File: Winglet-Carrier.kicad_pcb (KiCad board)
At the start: 4 copper layers, 80 x 60 mm, 69 parts, among them J1 1775862-2, J2 USB4105-GF-A-060, J3 USB4105-GF-A-060, J4 Pins_2.54_1x2, J5 Pins_2.54_1x2, M1 Mount_M3, M2 Mount_M3, M3 Mount_M3, M4 Mount_M3, M5 MM60-EZH039-B5-R850, Q1 2N7002-7-F, U1 USBLC6-2SC6, U2 USBLC6-2SC6, U3 STM32F072CxUx, U4 AP22804AW5-7, U5 AP62301WU-7, Y1 ECS-160-10-37-RWM-TR

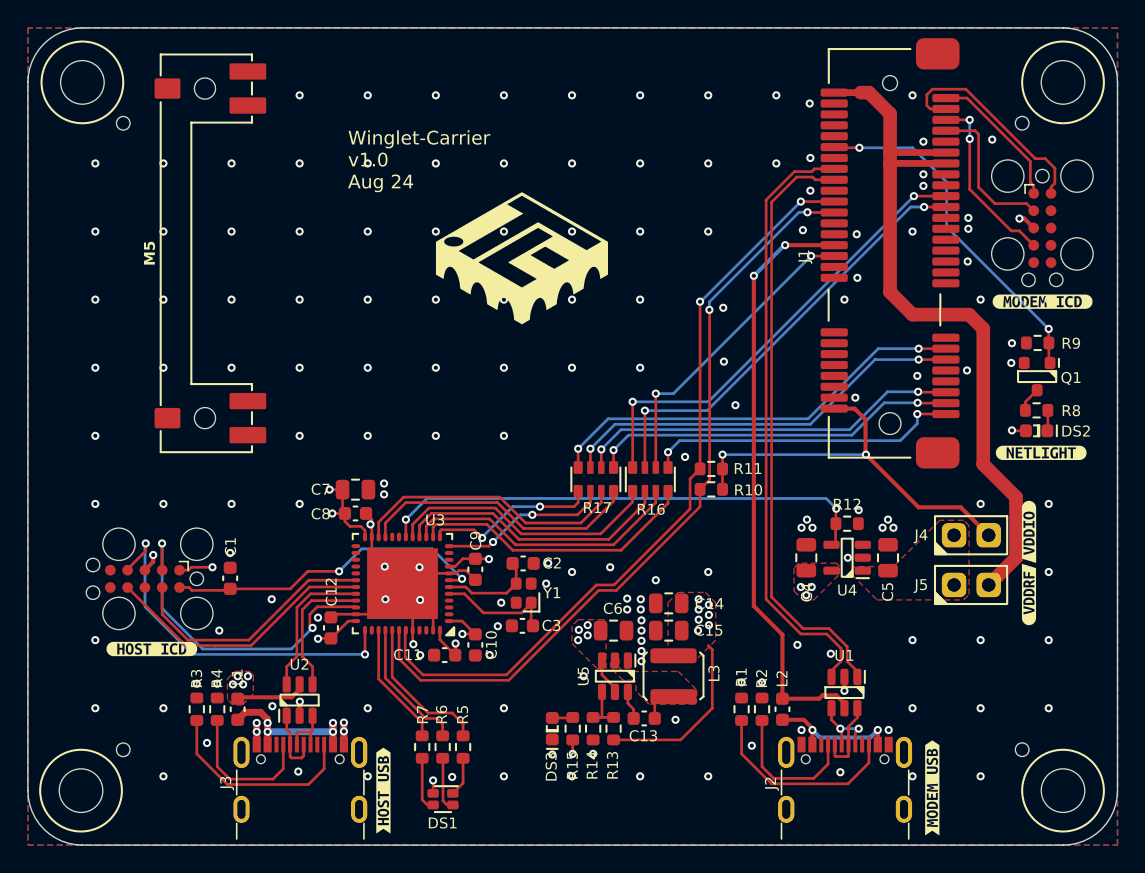
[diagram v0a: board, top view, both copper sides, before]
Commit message: Reannotate components
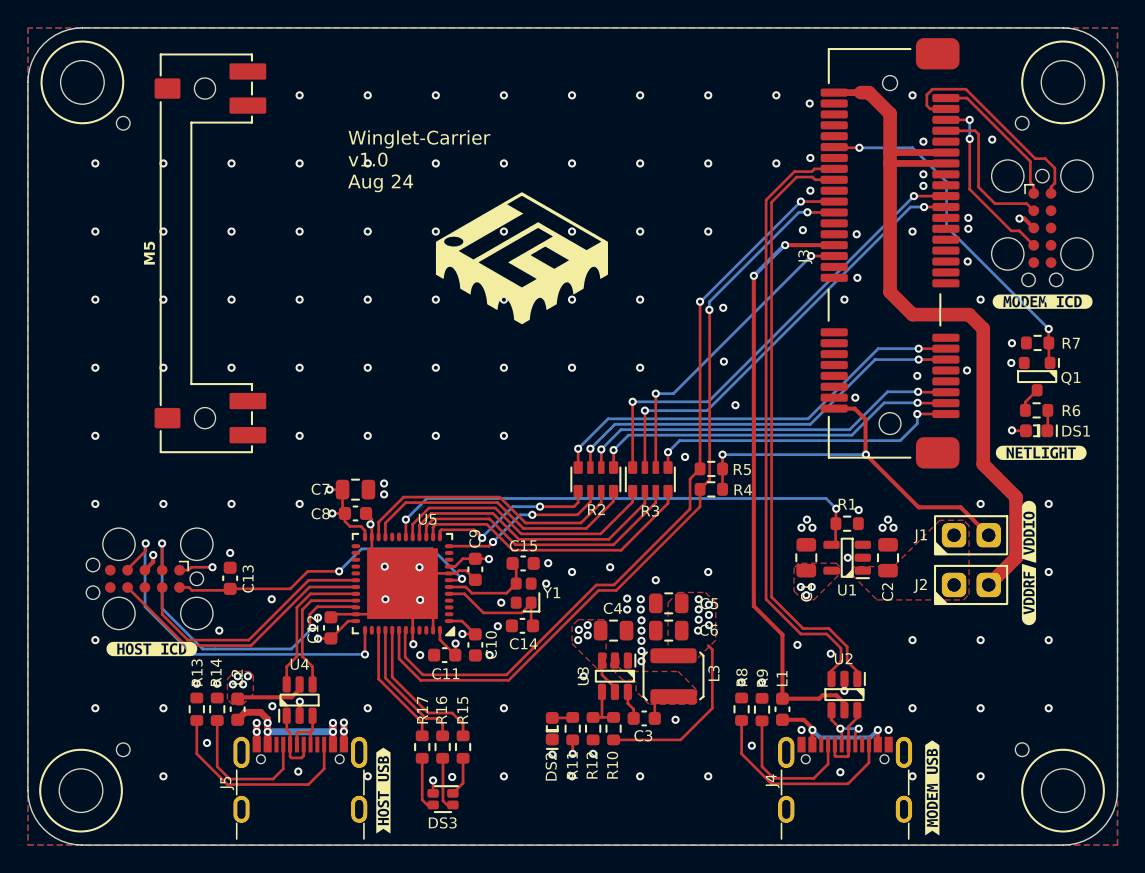
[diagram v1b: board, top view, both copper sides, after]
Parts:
- removed the J2 at (110.0, 106.3)
- removed the R1 at (102.4, 100.0)
- removed the R2 at (103.9, 100.0)
- removed the U1 at (110.0, 98.8)
- added J4: USB4105-GF-A-060, J_Connector:USB_C_USB4105-GF-A-060, F.Cu at (110.0, 106.3)
- added R8: 5K1, R_Resistor:R_0603, F.Cu at (102.4, 100.0)
- added R9: 5K1, R_Resistor:R_0603, F.Cu at (103.9, 100.0)
- added U2: USBLC6-2SC6, U_IC:SOT23_6, F.Cu at (110.0, 99.0)
- renumbered C4 to C1, C1 to C13, C3 to C14, C2 to C15, C5 to C2, C13 to C3, C6 to C4, C14 to C5, C15 to C6, DS2 to DS1, DS3 to DS2, DS1 to DS3, J4 to J1, J5 to J2, J1 to J3, J3 to J5, L2 to L1, L1 to L2, N3 to N1, N4 to N2, N5 to N3, N6 to N4, N1 to N5, N2 to N6, R12 to R1, R13 to R10, R15 to R11, R14 to R12, R3 to R13, R4 to R14, R5 to R15, R6 to R16, R7 to R17, R17 to R2, R16 to R3, R10 to R4, R11 to R5, R8 to R6, R9 to R7, U4 to U1, U5 to U3, U2 to U4, U3 to U5
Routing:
- net Net-(J4-CC2): track 0.00 -> 14.7 mm
- net Net-(J2-CC2): track 14.7 -> 0.00 mm
- net Net-(J4-CC1): track 0.00 -> 10.5 mm
- net Net-(J2-CC1): track 10.5 -> 0.00 mm
- net Net-(J4-D--PadA7): track 0.00 -> 5.63 mm
- net Net-(J2-D--PadA7): track 5.63 -> 0.00 mm
- net Net-(J4-D+-PadA6): track 0.00 -> 5.60 mm, vias 0 -> 2
- net Net-(J2-D+-PadA6): track 5.60 -> 0.00 mm, vias 2 -> 0
